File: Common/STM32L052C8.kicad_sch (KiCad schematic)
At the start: 14 parts

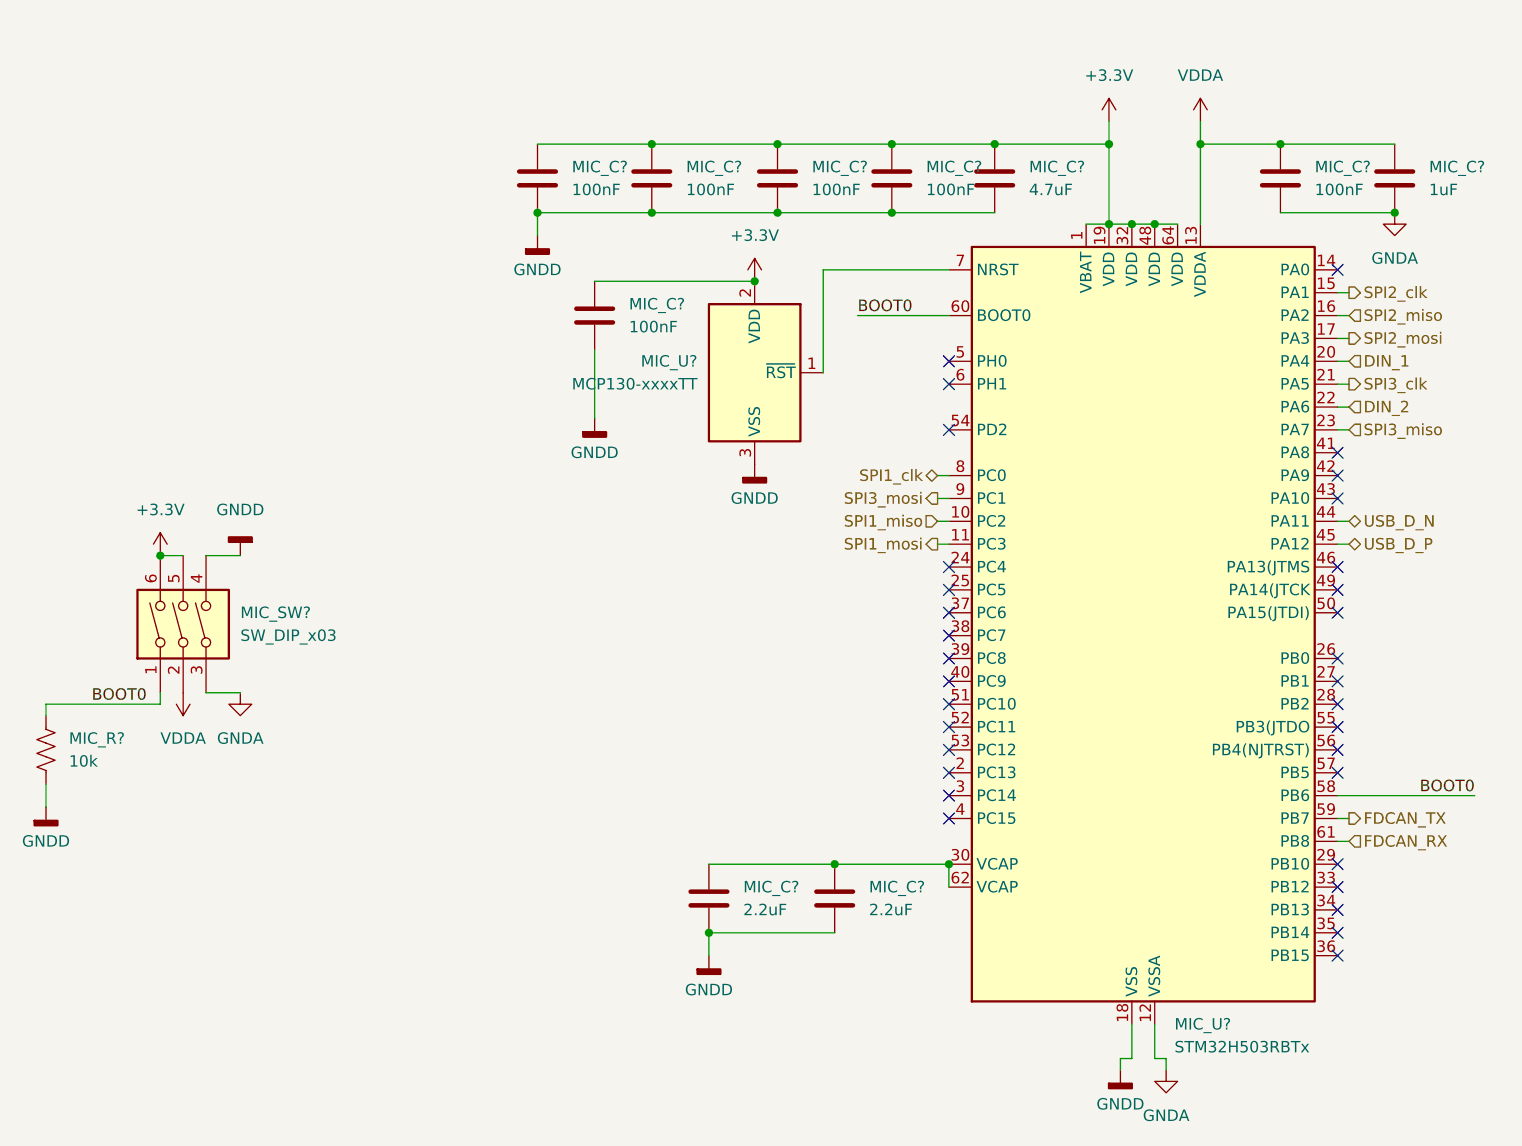
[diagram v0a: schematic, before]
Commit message: Updated Common Microcontroller Schematic
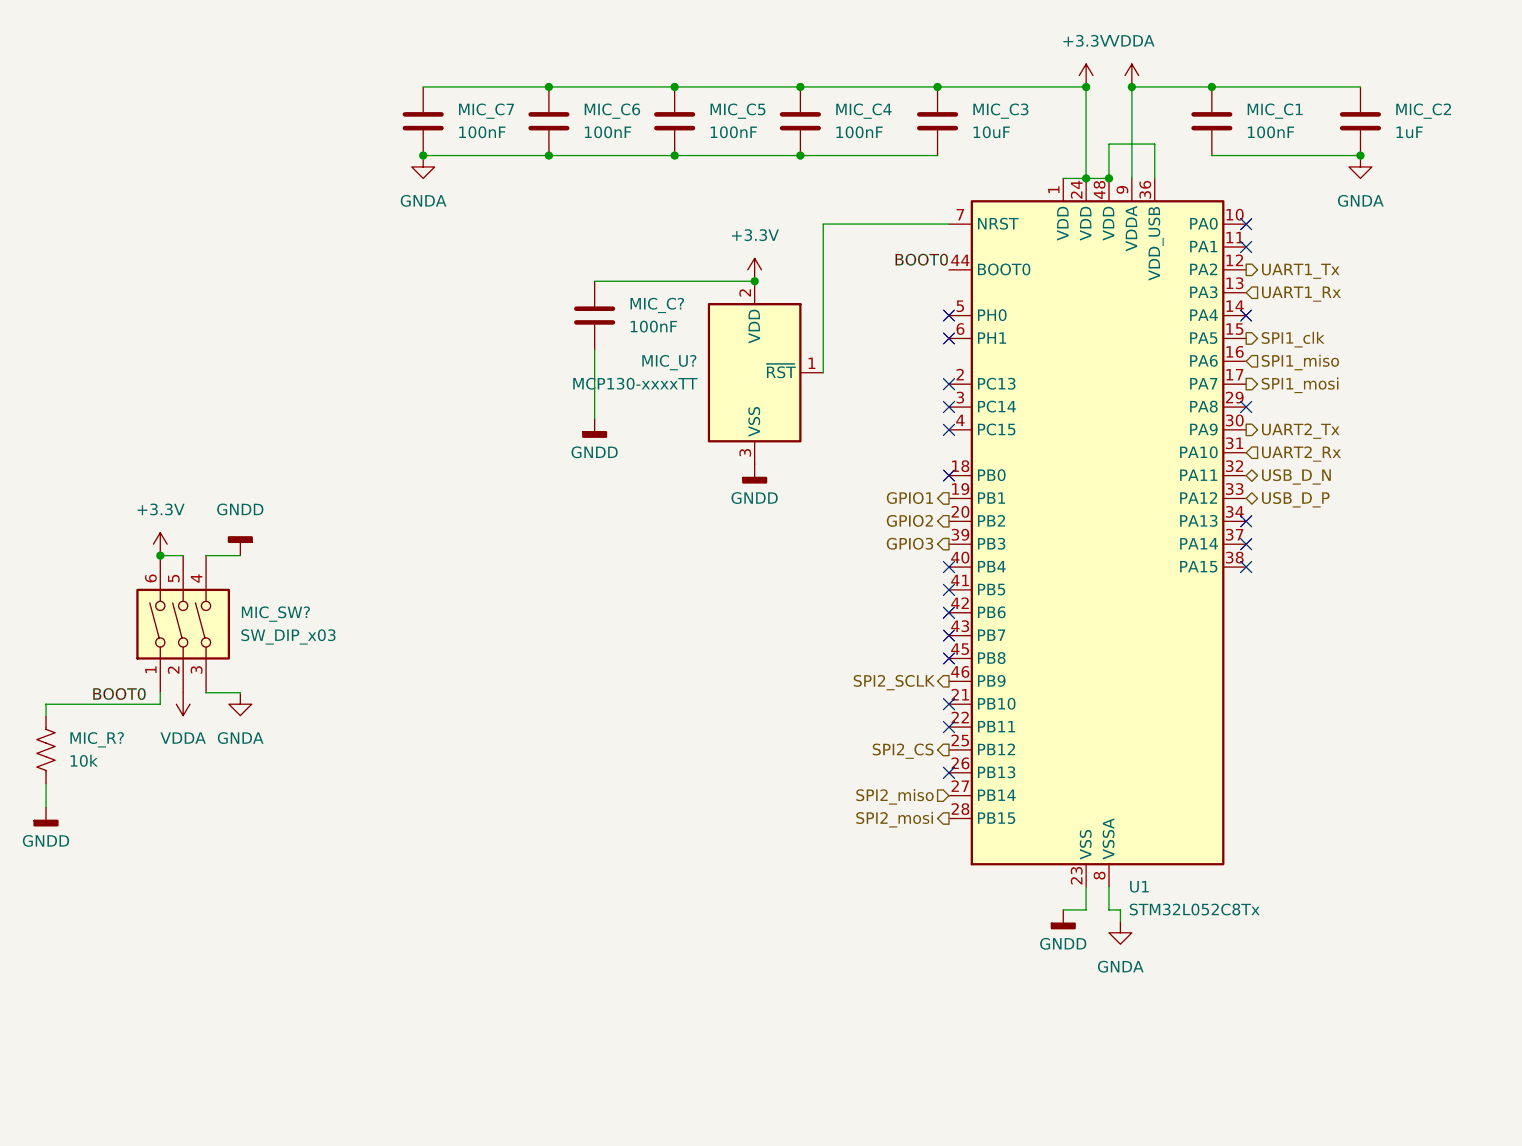
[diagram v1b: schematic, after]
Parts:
- removed MIC_C? (x2): 2.2uF, Capacitor_SMD:C_0603_1608Metric_Pad1.08x0.95mm_HandSolder, symbol Device:C
- removed MIC_C?: 1uF, Capacitor_SMD:C_0603_1608Metric_Pad1.08x0.95mm_HandSolder, symbol Device:C
- removed MIC_C? (x5): 100nF, Capacitor_SMD:C_0603_1608Metric_Pad1.08x0.95mm_HandSolder, symbol Device:C
- removed MIC_C?: 4.7uF, Capacitor_SMD:C_0603_1608Metric_Pad1.08x0.95mm_HandSolder, symbol Device:C
- removed MIC_U?: STM32H503RBTx, Package_QFP:LQFP-64_10x10mm_P0.5mm, symbol MCU_ST_STM32H5:STM32H503RBTx
- added MIC_C1, MIC_C4, MIC_C5, MIC_C6, MIC_C7: 100nF, Capacitor_SMD:C_0603_1608Metric_Pad1.08x0.95mm_HandSolder, symbol Device:C
- added MIC_C2: 1uF, Capacitor_SMD:C_0603_1608Metric_Pad1.08x0.95mm_HandSolder, symbol Device:C
- added MIC_C3: 10uF, Capacitor_SMD:C_0603_1608Metric_Pad1.08x0.95mm_HandSolder, symbol Device:C
- added U1: STM32L052C8Tx, Package_QFP:LQFP-48_7x7mm_P0.5mm, symbol MCU_ST_STM32L0:STM32L052C8Tx
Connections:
- net +3.3V: now also MIC_C3.1, MIC_C4.1, MIC_C5.1, MIC_C6.1, MIC_C7.1, U1.1 (VDD), U1.24 (VDD), U1.36 (VDD_USB), U1.48 (VDD)
- net BOOT0: now also U1.44 (BOOT0)
- net GNDA: now also MIC_C1.2, MIC_C2.2, MIC_C3.2, MIC_C4.2, MIC_C5.2, MIC_C6.2, MIC_C7.2, U1.8 (VSSA)
- net GNDD: now also U1.23 (VSS), U1.35 (VSS), U1.47 (VSS)
- net SPI1_clk: now also U1.15 (PA5)
- net SPI1_miso: now also U1.16 (PA6)
- net SPI1_mosi: now also U1.17 (PA7)
- net SPI2_miso: now also U1.27 (PB14)
- net SPI2_mosi: now also U1.28 (PB15)
- net USB_D_N: now also U1.32 (PA11)
- net USB_D_P: now also U1.33 (PA12)
- net VDDA: now also MIC_C1.1, MIC_C2.1, U1.9 (VDDA)
- net at MIC_U?.1 (~{RST}): now also U1.7 (NRST)
- new net GPIO1: U1.19 (PB1)
- new net GPIO2: U1.20 (PB2)
- new net GPIO3: U1.39 (PB3)
- new net SPI2_CS: U1.25 (PB12)
- new net SPI2_SCLK: U1.46 (PB9)
- new net UART1_Rx: U1.13 (PA3)
- new net UART1_Tx: U1.12 (PA2)
- new net UART2_Rx: U1.31 (PA10)
- new net UART2_Tx: U1.30 (PA9)
- no-connect marks 33 -> 21

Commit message: VDD Capacitors
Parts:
- removed MIC_C7: 100nF, Capacitor_SMD:C_0603_1608Metric_Pad1.08x0.95mm_HandSolder, symbol Device:C
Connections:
- net +3.3V: no longer U1.36 (VDD_USB)
- net GNDA: no longer MIC_C3.2, MIC_C4.2, MIC_C5.2, MIC_C6.2
- net GNDD: now also MIC_C3.2, MIC_C4.2, MIC_C5.2, MIC_C6.2
